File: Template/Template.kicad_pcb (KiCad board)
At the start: 2 copper layers, 99.9 x 99.9 mm, 1 part, among them J1 Bus_ISA_8bit

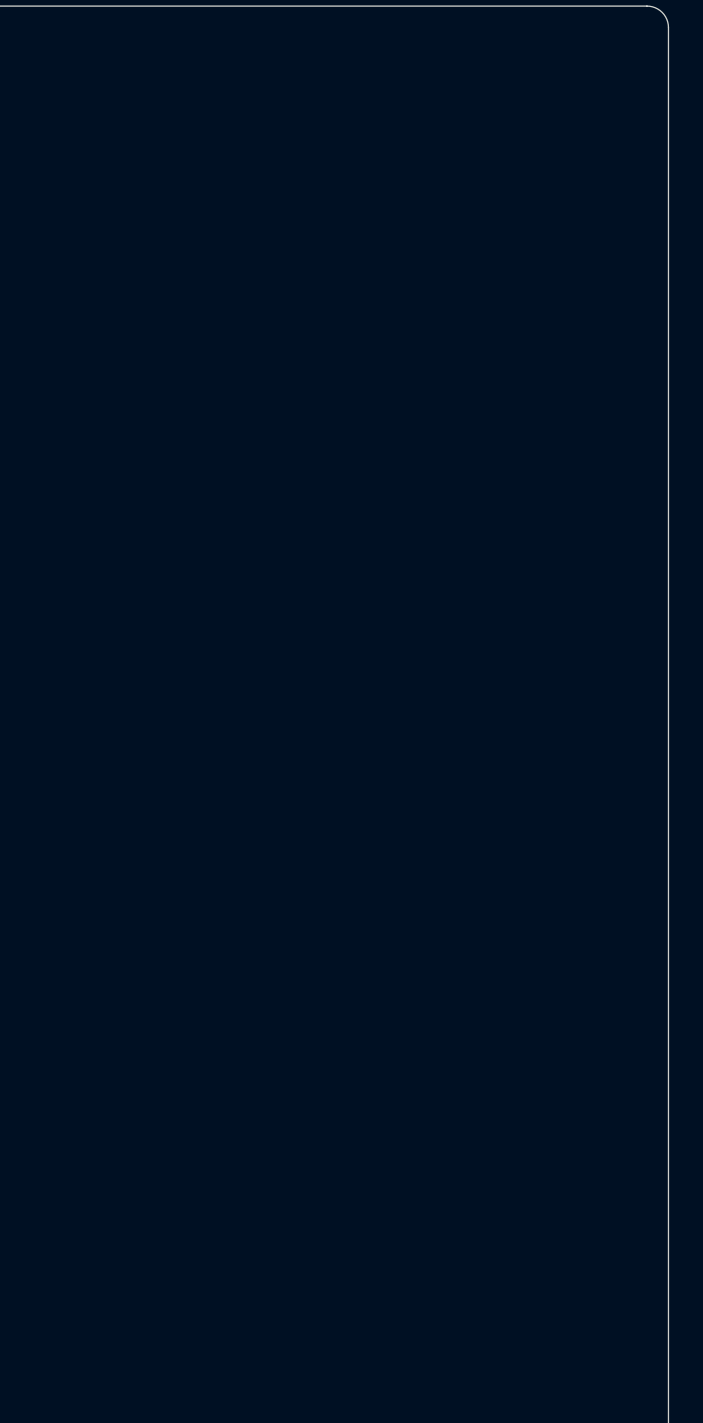
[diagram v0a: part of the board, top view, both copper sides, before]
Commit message: Template: Add mounting holes for IDE to CF adapter.
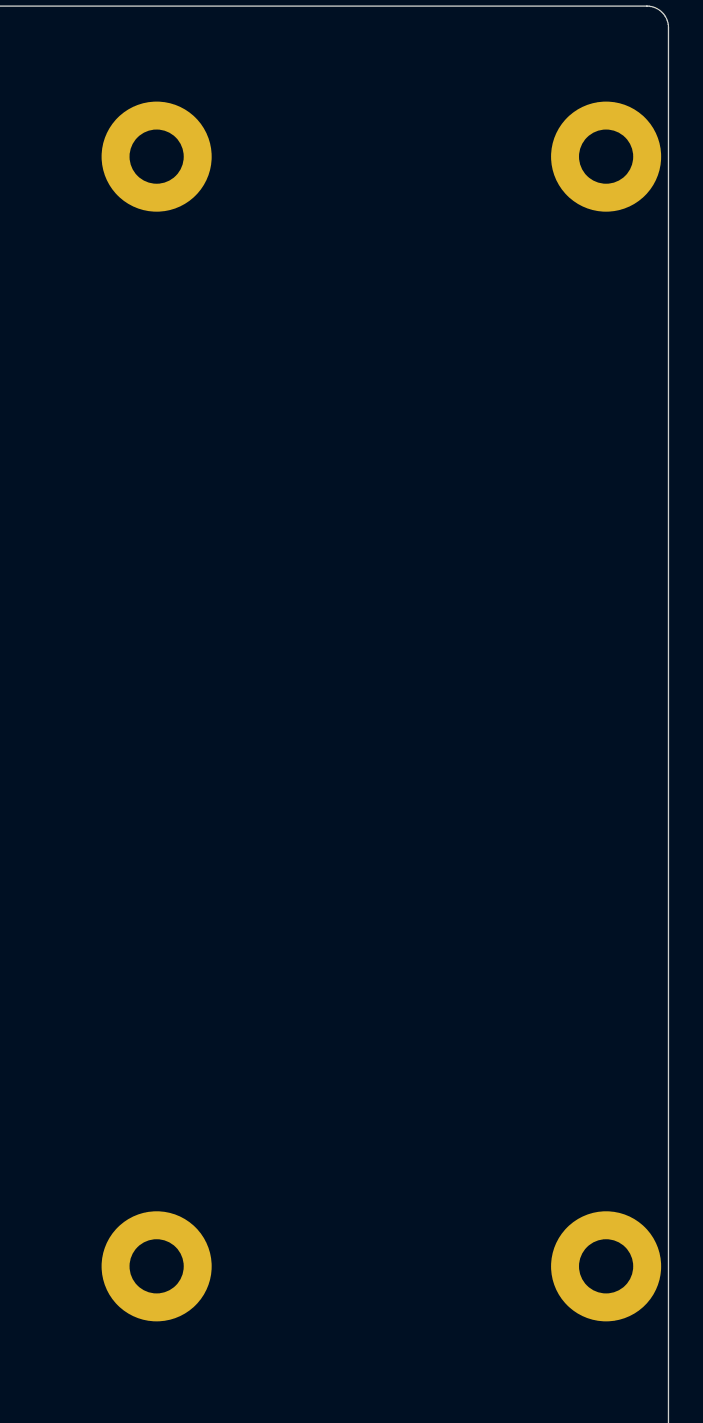
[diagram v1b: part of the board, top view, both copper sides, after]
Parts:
- added MH1: MH, MountingHole:MountingHole_3.5mm_Pad, F.Cu at (166.4, 51.2)
- added MH2: MH, MountingHole:MountingHole_3.5mm_Pad, F.Cu at (192.9, 51.2)
- added MH3: MH, MountingHole:MountingHole_3.5mm_Pad, F.Cu at (166.4, 116.7)
- added MH4: MH, MountingHole:MountingHole_3.5mm_Pad, F.Cu at (192.9, 116.7)
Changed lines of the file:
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@@
     (tracks 0)
     (zones 0)
-    (modules 1)
+    (modules 5)
     (nets 63)
   )
@@
     (pad_to_mask_clearance 0)
     (aux_axis_origin 0 0)
-    (visible_elements FFFFFF7F)
+    (visible_elements 7FFFFFFF)
     (pcbplotparams
       (layerselection 0x010fc_ffffffff)
@@
     (add_net "Net-(J1-Pad9)")
   )
+  (module MountingHole:MountingHole_3.5mm_Pad (layer F.Cu)
+    (at 166.37 116.713)
+    (descr "Mounting Hole 3.5mm")
+    (tags "mounting hole 3.5mm")
+    (attr virtual)
+    (fp_text reference MH3 (at 0 -4.5) (layer F.SilkS) hide
+      (effects (font (size 1 1) (thickness 0.15)))
+    )
+    (fp_text value MH (at 5.08 0) (layer F.Fab)
+      (effects (font (size 1 1) (thickness 0.15)))
+    )
+    (fp_text user %R (at 0.3 0) (layer F.Fab)
+      (effects (font (size 1 1) (thickness 0.15)))
+    )
+    (fp_circle (center 0 0) (end 3.75 0) (layer F.CrtYd) (width 0.05))
+    (pad "" thru_hole circle (at 0 0) (size 6.5 6.5) (drill 3.2) (layers *.Cu *.Mask))
+  )
+  (module MountingHole:MountingHole_3.5mm_Pad (layer F.Cu)
+    (at 166.37 51.181)
+    (descr "Mounting Hole 3.5mm")
+    (tags "mounting hole 3.5mm")
+    (attr virtual)
+    (fp_text reference MH1 (at 0 -4.5) (layer F.SilkS) hide
+      (effects (font (size 1 1) (thickness 0.15)))
+    )
+    (fp_text value MH (at 5.08 0) (layer F.Fab)
+      (effects (font (size 1 1) (thickness 0.15)))
+    )
+    (fp_text user %R (at 0.3 0) (layer F.Fab)
+      (effects (font (size 1 1) (thickness 0.15)))
+    )
+    (fp_circle (center 0 0) (end 3.75 0) (layer F.CrtYd) (width 0.05))
+    (pad "" thru_hole circle (at 0 0) (size 6.5 6.5) (drill 3.2) (layers *.Cu *.Mask))
+  )
+  (module MountingHole:MountingHole_3.5mm_Pad (layer F.Cu)
+    (at 192.913 116.713)
+    (descr "Mounting Hole 3.5mm")
+    (tags "mounting hole 3.5mm")
+    (attr virtual)
+    (fp_text reference MH4 (at 0 -4.5) (layer F.SilkS) hide
+      (effects (font (size 1 1) (thickness 0.15)))
+    )
+    (fp_text value MH (at 5.08 0) (layer F.Fab)
+      (effects (font (size 1 1) (thickness 0.15)))
+    )
+    (fp_circle (center 0 0) (end 3.75 0) (layer F.CrtYd) (width 0.05))
+    (fp_text user %R (at 0.3 0) (layer F.Fab)
+      (effects (font (size 1 1) (thickness 0.15)))
+    )
+    (pad "" thru_hole circle (at 0 0) (size 6.5 6.5) (drill 3.2) (layers *.Cu *.Mask))
+  )
+  (module MountingHole:MountingHole_3.5mm_Pad (layer F.Cu)
+    (at 192.913 51.181)
+    (descr "Mounting Hole 3.5mm")
+    (tags "mounting hole 3.5mm")
+    (attr virtual)
+    (fp_text reference MH2 (at 0 -4.5) (layer Dwgs.User)
+      (effects (font (size 1 1) (thickness 0.15)))
+    )
+    (fp_text value MH (at 5.08 0) (layer F.Fab)
+      (effects (font (size 1 1) (thickness 0.15)))
+    )
+    (fp_circle (center 0 0) (end 3.75 0) (layer F.CrtYd) (width 0.05))
+    (fp_text user %R (at 0.3 0) (layer F.Fab)
+      (effects (font (size 1 1) (thickness 0.15)))
+    )
+    (pad "" thru_hole circle (at 0 0) (size 6.5 6.5) (drill 3.2) (layers *.Cu *.Mask))
+  )
   (module 00Custom:BUS_XT (layer F.Cu)
     (at 175.26 138.43)
@@
     (tags "BUS ISA AT Edge connector")
     (attr virtual)
-    (fp_text reference J1 (at -26.035 -6.99) (layer F.SilkS) hide
-      (effects (font (size 1 1) (thickness 0.15)))
-    )
-    (fp_text value Bus_ISA_8bit (at -34.29 -6.985) (layer F.Fab)
+    (fp_text reference J1 (at -40.767 5.461) (layer F.SilkS) hide
+      (effects (font (size 1 1) (thickness 0.15)))
+    )
+    (fp_text value Bus_ISA_8bit (at -34.036 5.461) (layer F.Fab)
       (effects (font (size 1 1) (thickness 0.15)))
     )
@@
     (effects (font (size 1 1) (thickness 0.15)))
   )
-  (gr_text "ISA bus dimensions mostly taken from the \nIBM 5150 Technical Refererence Manual." (at 144.78 65.405) (layer Cmts.User)
+  (gr_text "ISA bus dimensions mostly taken from the \nIBM 5150 Technical Refererence Manual." (at 146.558 38.735) (layer Cmts.User)
     (effects (font (size 1 1) (thickness 0.15)))
   )
-  (gr_text "The outline is aligned to 0.127mm grid and is sized to fit \nwithin the magic 100mm by 100mm size limit set by \ncertain PCB manufaturers for very inexpensive boards." (at 144.145 57.785) (layer Cmts.User)
+  (gr_text "The outline is aligned to 0.127mm grid and is sized to fit \nwithin the magic 100mm by 100mm size limit set by \ncertain PCB manufaturers for very inexpensive boards." (at 145.923 31.115) (layer Cmts.User)
     (effects (font (size 1 1) (thickness 0.15)))
   )

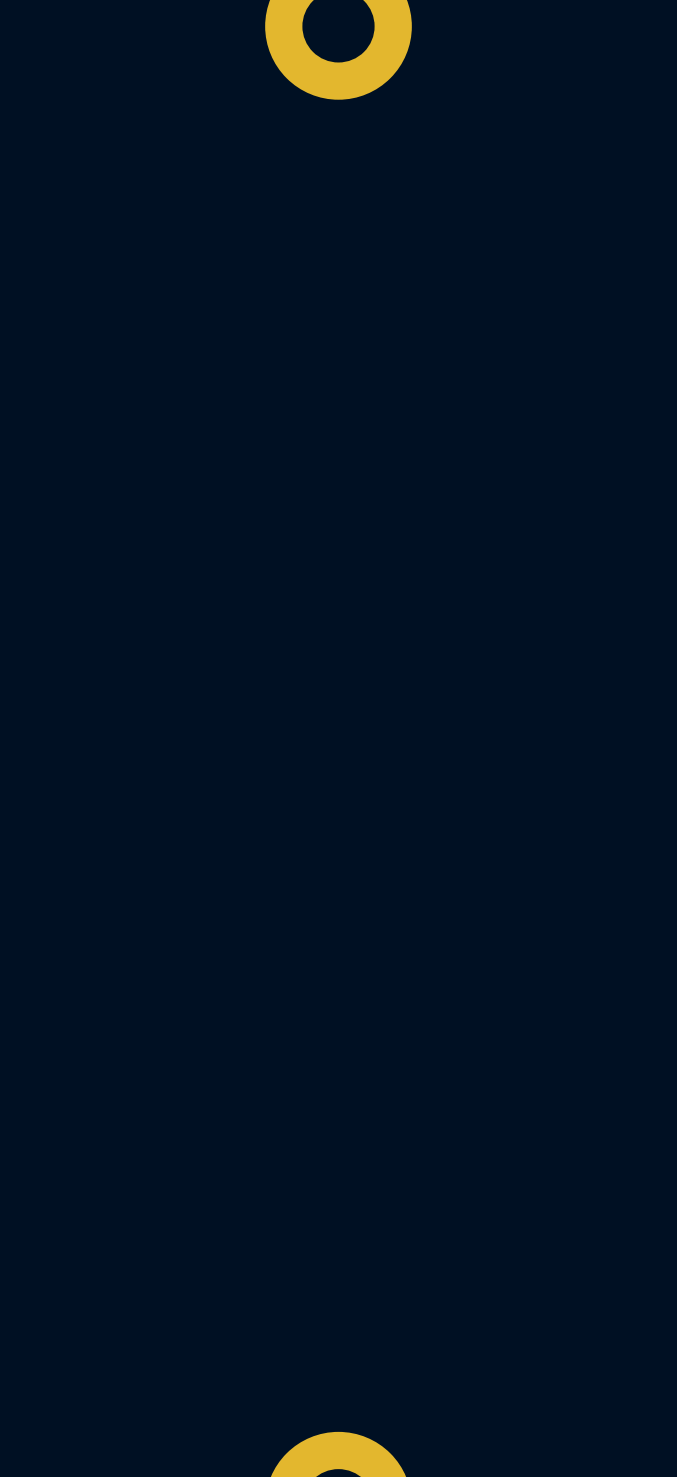
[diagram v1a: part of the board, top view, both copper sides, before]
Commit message: Add IDE/ATA connector to Template.
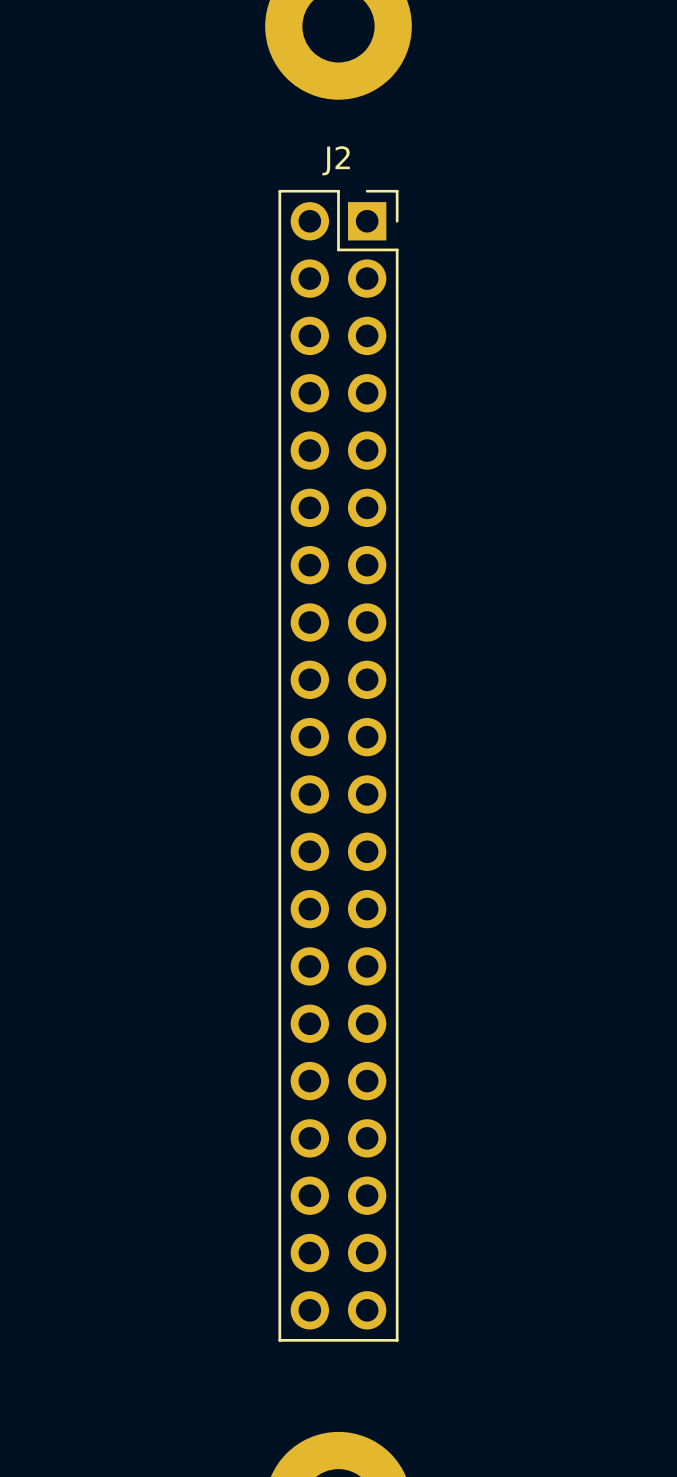
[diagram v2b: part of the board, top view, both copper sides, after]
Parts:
- added J2: IDE_CONNECTOR, Connector_PinSocket_2.54mm:PinSocket_2x20_P2.54mm_Vertical, F.Cu at (167.6, 59.8)

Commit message: Add global labels to the ISA bus connector,
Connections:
- net Net-(J1-Pad11) renamed ~MEMW
- net Net-(J1-Pad12) renamed ~MEMR
- net Net-(J1-Pad13) renamed ~IOW
- net Net-(J1-Pad14) renamed ~IOR
- net Net-(J1-Pad15) renamed ~DACK3
- net Net-(J1-Pad16) renamed DRQ3
- net Net-(J1-Pad17) renamed ~DACK1
- net Net-(J1-Pad18) renamed DRQ1
- net Net-(J1-Pad19) renamed ~DACK0
- net Net-(J1-Pad2) renamed RESET
- net Net-(J1-Pad20) renamed CLK
- net Net-(J1-Pad21) renamed IRQ7
- net Net-(J1-Pad22) renamed IRQ6
- net Net-(J1-Pad23) renamed IRQ5
- net Net-(J1-Pad24) renamed IRQ4
- net Net-(J1-Pad25) renamed IRQ3
- net Net-(J1-Pad26) renamed ~DACK2
- net Net-(J1-Pad27) renamed TC
- net Net-(J1-Pad28) renamed ALE
- net Net-(J1-Pad30) renamed OSC
- net Net-(J1-Pad32) renamed ~IO_CH_CK
- net Net-(J1-Pad33) renamed D7
- net Net-(J1-Pad34) renamed D6
- net Net-(J1-Pad35) renamed D5
- net Net-(J1-Pad36) renamed D4
- net Net-(J1-Pad37) renamed D3
- net Net-(J1-Pad38) renamed D2
- net Net-(J1-Pad39) renamed D1
- net Net-(J1-Pad4) renamed IRQ2
- net Net-(J1-Pad40) renamed D0
- net Net-(J1-Pad41) renamed IOCHRDY
- net Net-(J1-Pad42) renamed AEN
- net Net-(J1-Pad43) renamed A19
- net Net-(J1-Pad44) renamed A18
- net Net-(J1-Pad45) renamed A17
- net Net-(J1-Pad46) renamed A16
- net Net-(J1-Pad47) renamed A15
- net Net-(J1-Pad48) renamed A14
- net Net-(J1-Pad49) renamed A13
- net Net-(J1-Pad5) renamed -5V
- net Net-(J1-Pad50) renamed A12
- net Net-(J1-Pad51) renamed A11
- net Net-(J1-Pad52) renamed A10
- net Net-(J1-Pad53) renamed A09
- net Net-(J1-Pad54) renamed A08
- net Net-(J1-Pad55) renamed A07
- net Net-(J1-Pad56) renamed A06
- net Net-(J1-Pad57) renamed A05
- net Net-(J1-Pad58) renamed A04
- net Net-(J1-Pad59) renamed A03
- net Net-(J1-Pad6) renamed DRQ2
- net Net-(J1-Pad60) renamed A02
- net Net-(J1-Pad61) renamed A01
- net Net-(J1-Pad62) renamed A00
- net Net-(J1-Pad7) renamed -12V
- net Net-(J1-Pad9) renamed +12V
- J1 pad 1: Net-(J1-Pad1) -> GND
- J1 pad 10: Net-(J1-Pad10) -> GND
- J1 pad 29: Net-(J1-Pad29) -> VCC
- J1 pad 3: Net-(J1-Pad3) -> VCC
- J1 pad 31: Net-(J1-Pad31) -> GND

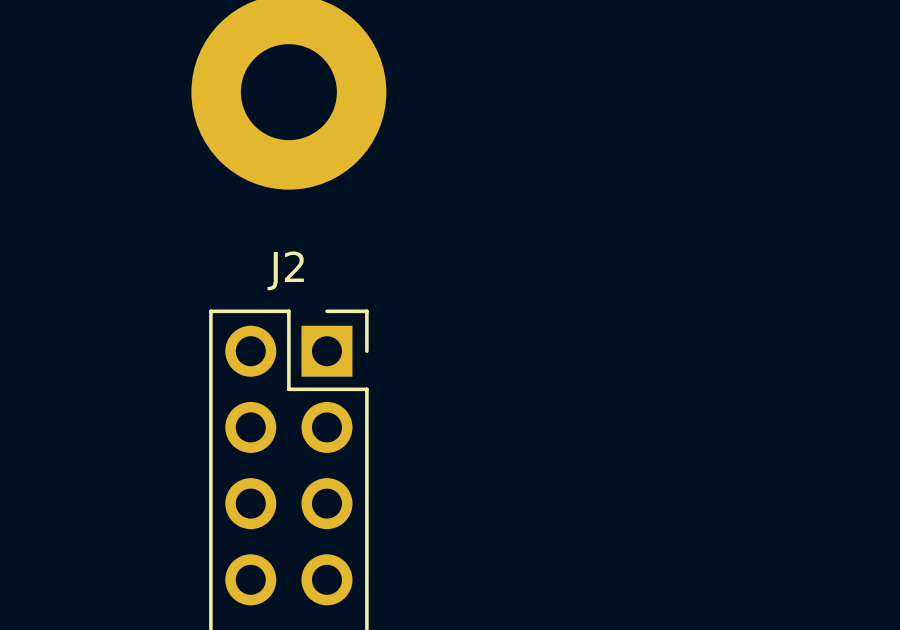
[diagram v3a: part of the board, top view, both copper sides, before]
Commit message: Add power for CF adapter to Template and CF-Super-Lite.
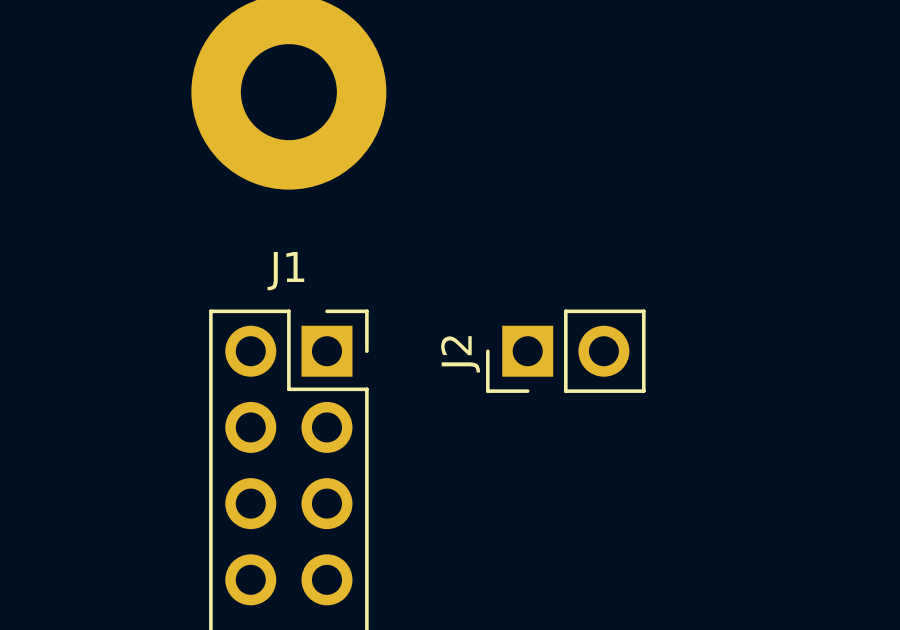
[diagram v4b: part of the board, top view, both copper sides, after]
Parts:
- added J2: CF Adapter Power, Connector_PinHeader_2.54mm:PinHeader_1x02_P2.54mm_Vertical, F.Cu at (174.3, 59.8)
- renumbered J2 to J1, J1 to J3
